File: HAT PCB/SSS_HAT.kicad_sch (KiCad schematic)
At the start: 26 parts, among them J1 ESP32_Connector_0, J2 ESP32_Connector_1, J3 CAN, J4 CAN, J5 I2C, J6 ADC_0, J7 ADC_1, SW1 I2C, SW2 IMU_SPI_Pullup, U1 TJA1051T, U2 MCP3422Axx-xMS, U3 LSM9DS1

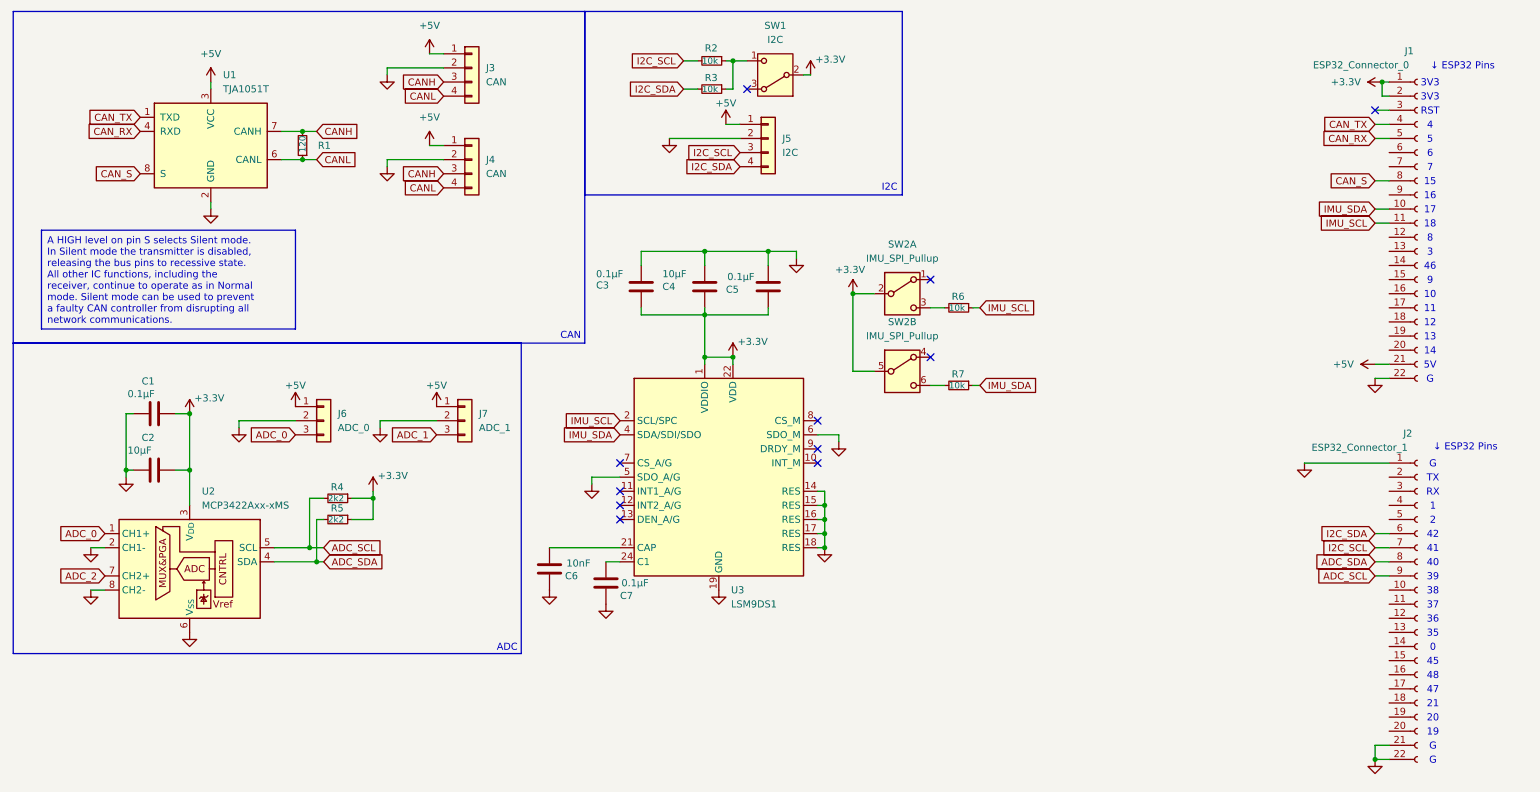
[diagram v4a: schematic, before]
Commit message: Routed PCB & Replaced IMU for ICM-42688-P
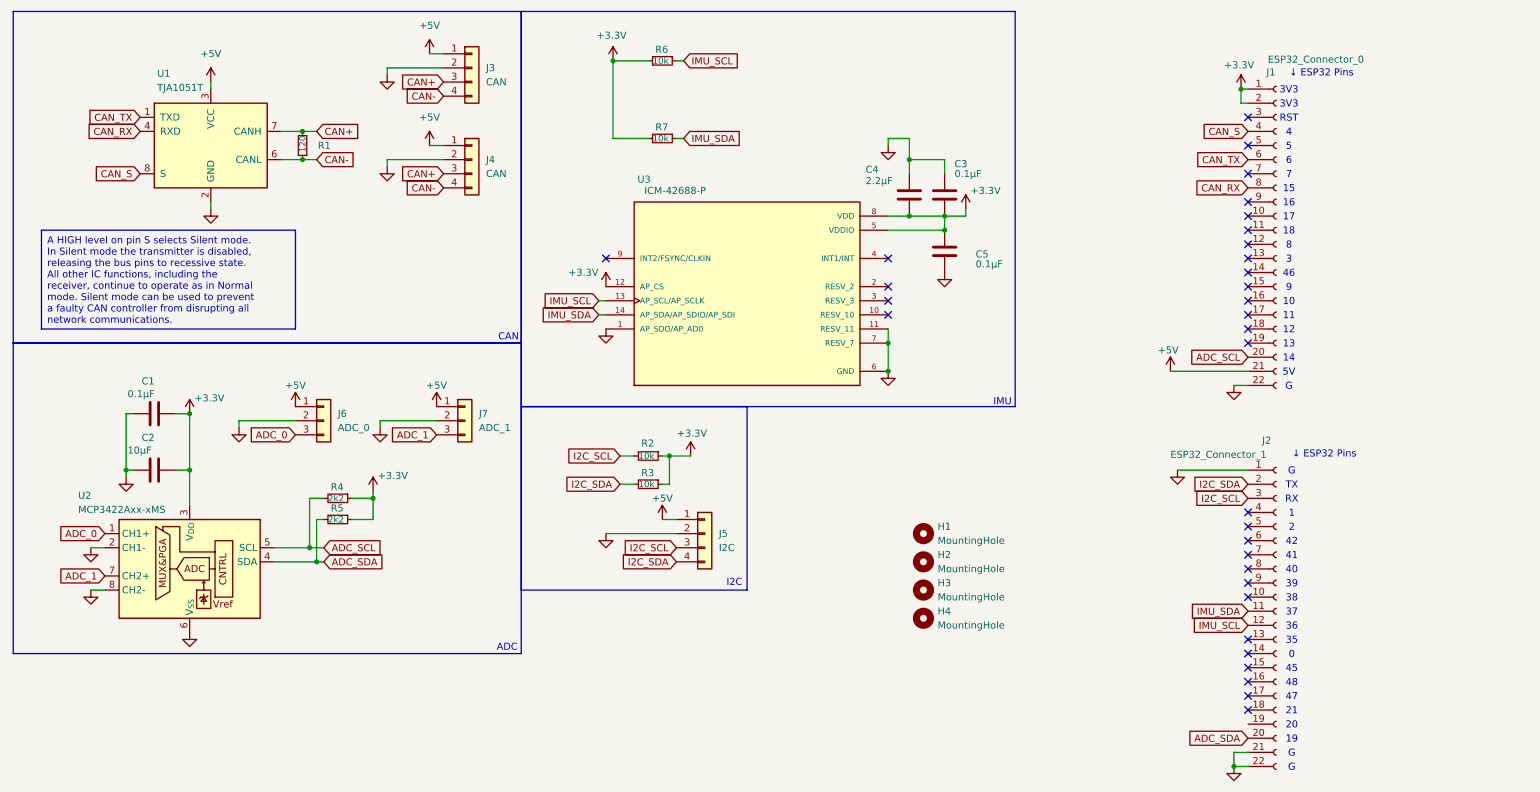
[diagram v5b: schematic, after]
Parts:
- removed C6: 10nF, Capacitor_SMD:C_0402_1005Metric_Pad0.74x0.62mm_HandSolder, symbol Device:C
- removed C7: 0.1μF, Capacitor_SMD:C_0402_1005Metric_Pad0.74x0.62mm_HandSolder, symbol Device:C
- removed SW1: I2C, Button_Switch_SMD:Nidec_Copal_CAS-120A, symbol Switch:SW_Nidec_CAS-120A1
- removed SW2: IMU_SPI_Pullup, Button_Switch_SMD:SW_DPDT_CK_JS202011JCQN, symbol Switch:SW_DPDT_x2
- removed U3: LSM9DS1, Package_LGA:LGA-24L_3x3.5mm_P0.43mm, symbol Sensor_Motion:LSM9DS1
- added H1, H2, H3, H4: MountingHole, MountingHole:MountingHole_2.7mm_M2.5, symbol Mechanical:MountingHole
- added U3: ICM-42688-P, ICM-42688-P:PQFN50P300X250X97-14N, symbol ICM-42688-P:ICM-42688-P
- C4: value 10μF -> 2.2μF
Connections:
- net ADC_2 is gone; now on net ADC_1: U2.7 (CH2+)
- net +3.3V: now also C5.1, R2.1, R3.1, R6.2, R7.2, U3.12 (AP_CS), U3.5 (VDDIO), U3.8 (VDD); no longer C5.2
- net ADC_SCL: now also J1.20 (Pin_20); no longer J2.9 (Pin_9)
- net ADC_SDA: now also J2.20 (Pin_20); no longer J2.8 (Pin_8)
- net CAN_RX: now also J1.8 (Pin_8); no longer J1.5 (Pin_5)
- net CAN_S: now also J1.4 (Pin_4); no longer J1.8 (Pin_8)
- net CAN_TX: now also J1.6 (Pin_6); no longer J1.4 (Pin_4)
- net GND: now also C5.2, U3.1 (AP_SDO/AP_AD0), U3.11 (RESV_11), U3.6 (GND), U3.7 (RESV_7); no longer C5.1
- net I2C_SCL: now also J2.3 (Pin_3); no longer J2.7 (Pin_7)
- net I2C_SDA: now also J2.2 (Pin_2); no longer J2.6 (Pin_6)
- net IMU_SCL: now also J2.12 (Pin_12), U3.13 (AP_SCL/AP_SCLK); no longer J1.11 (Pin_11)
- net IMU_SDA: now also J2.11 (Pin_11), U3.14 (AP_SDA/AP_SDIO/AP_SDI); no longer J1.10 (Pin_10)
- net CANH renamed CAN+
- net CANL renamed CAN-
- no-connect marks 11 -> 32
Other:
- note added: "IMU"
- moved on the sheet: J1, J2, R6, R7

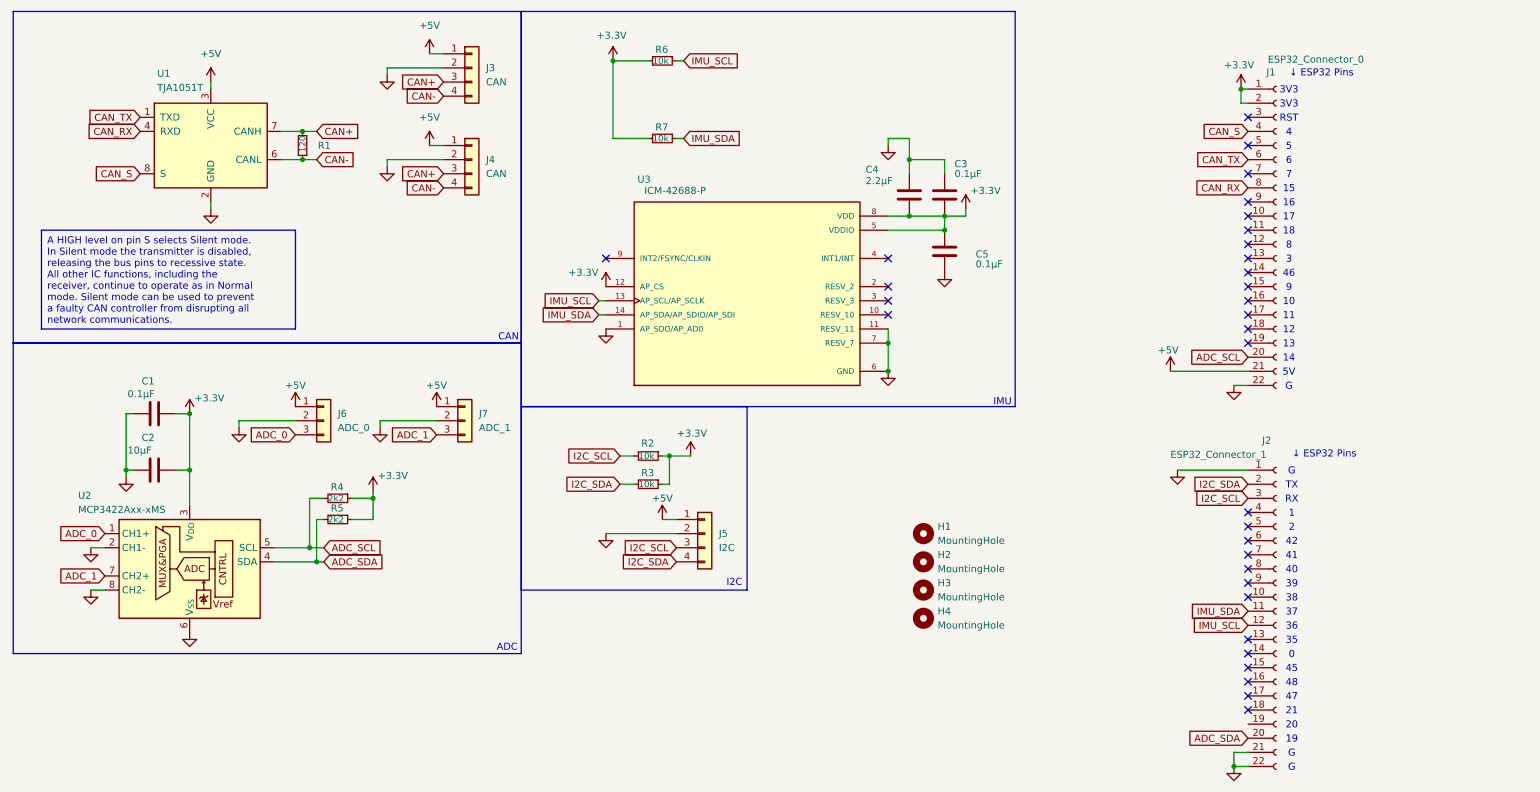
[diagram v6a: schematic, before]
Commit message: Added ADS8320EB/250 ADC
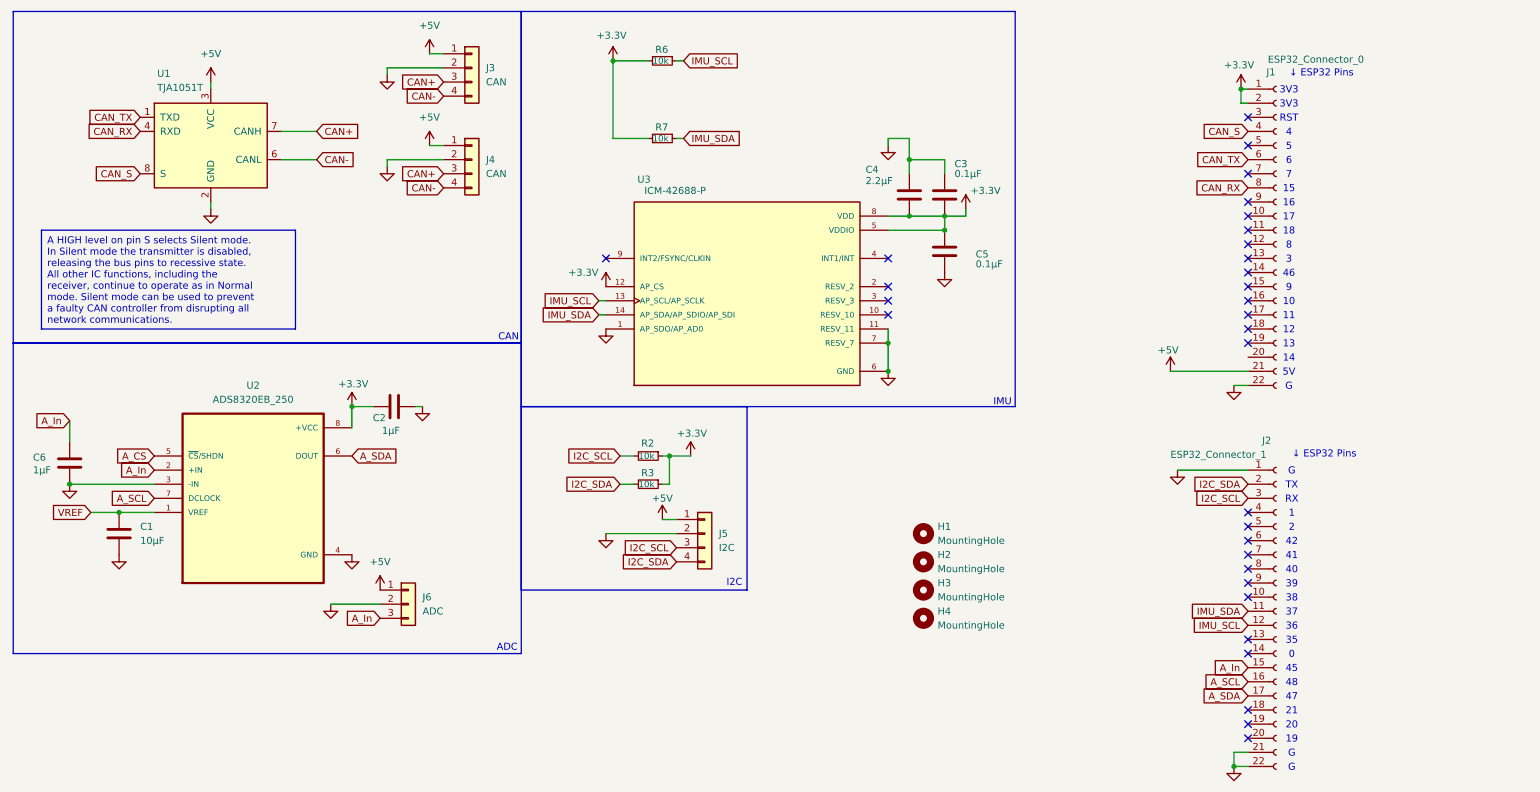
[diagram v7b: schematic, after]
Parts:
- removed J7: ADC_1, Connector_Molex:Molex_Nano-Fit_105313-xx03_1x03_P2.50mm_Horizontal, symbol Connector_Generic:Conn_01x03
- removed R1: 120, Resistor_SMD:R_0402_1005Metric_Pad0.72x0.64mm_HandSolder, symbol Device:R_Small
- removed R4, R5: 2k2, Resistor_SMD:R_0402_1005Metric_Pad0.72x0.64mm_HandSolder, symbol Device:R_Small
- removed U2: MCP3422Axx-xMS, Package_SO:MSOP-8_3x3mm_P0.65mm, symbol Analog_ADC:MCP3422Axx-xMS
- added C6: 1μF, symbol Device:C
- added U2: ADS8320EB_250, ADS8320EB_250:SOP65P490X110-8N, symbol ADS8320EB:ADS8320EB_250
- C1: value 0.1μF -> 10μF; footprint Capacitor_SMD:C_0402_1005Metric_Pad0.74x0.62mm_HandSolder -> (none)
- C2: value 10μF -> 1μF; footprint Capacitor_SMD:C_0402_1005Metric_Pad0.74x0.62mm_HandSolder -> (none)
- J6: value ADC_0 -> ADC; footprint Connector_Molex:Molex_Nano-Fit_105313-xx03_1x03_P2.50mm_Horizontal -> (none)
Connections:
- net ADC_0 is gone; now on net A_In: J6.3 (Pin_3)
- net +3.3V: now also U2.8 (+VCC); no longer C1.1
- net GND: now also C6.2, U2.3 (-IN), U2.4 (GND)
- net A_In: now reaches J2.15 (Pin_15)
- net A_In: now also C6.1, U2.2 (+IN)
- net A_SCL: now reaches J2.16 (Pin_16)
- net A_SCL: now also U2.7 (DCLOCK)
- net A_SDA: now reaches J2.17 (Pin_17)
- net A_SDA: now also U2.6 (DOUT)
- net ADC_SCL: no longer names the net of J1.20 (Pin_20)
- net ADC_SDA: no longer names the net of J2.20 (Pin_20)
- new net A_CS: U2.5 (~{CS}/SHDN)
- new net VREF: C1.1, U2.1 (VREF)
- no-connect marks 32 -> 31

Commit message: Updated 3D model & readme.
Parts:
- removed J3, J4: CAN, Connector_Molex:Molex_Nano-Fit_105313-xx04_1x04_P2.50mm_Horizontal, symbol Connector_Generic:Conn_01x04
- removed J5: I2C, Connector_Molex:Molex_Nano-Fit_105313-xx04_1x04_P2.50mm_Horizontal, symbol Connector_Generic:Conn_01x04
- removed J6: ADC, symbol Connector_Generic:Conn_01x03
- removed R6, R7: 10k, Resistor_SMD:R_0402_1005Metric_Pad0.72x0.64mm_HandSolder, symbol Device:R_Small
- added J3, J4, J5: I2C, Connector_Hirose:Hirose_DF3EA-04P-2H_1x04-1MP_P2.00mm_Horizontal, symbol Connector_Generic_MountingPin:Conn_01x04_MountingPin
- added J6: ADC, Connector_Hirose:Hirose_DF3EA-03P-2H_1x03-1MP_P2.00mm_Horizontal, symbol Connector_Generic_MountingPin:Conn_01x03_MountingPin
- C1, C2, C6: footprint (none) -> Capacitor_SMD:C_0402_1005Metric_Pad0.74x0.62mm_HandSolder
- U2: footprint ADS8320EB_250:SOP65P490X110-8N -> ADS8320EB_250:DGK0008A_L
- renumbered R2 to R1, R3 to R2
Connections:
- net VREF is gone; now on net +3.3V: C1.1, U2.1 (VREF)
- net +3.3V: no longer U3.12 (AP_CS)
- net +5V: now also J3.1 (Pin_1), J4.1 (Pin_1), J5.1 (Pin_1), J6.1 (Pin_1)
- net A_CS: now also J2.7 (Pin_7)
- net A_In: now also J2.4 (Pin_4), J6.3 (Pin_3); no longer J2.15 (Pin_15)
- net A_SCL: now also J2.5 (Pin_5); no longer J2.16 (Pin_16)
- net A_SDA: now also J2.6 (Pin_6); no longer J2.17 (Pin_17)
- net CAN+: now also J3.4 (Pin_4), J4.4 (Pin_4)
- net CAN-: now also J3.3 (Pin_3), J4.3 (Pin_3)
- net CAN_RX: now also J1.17 (Pin_17); no longer J1.8 (Pin_8)
- net CAN_S: now also J1.18 (Pin_18); no longer J1.4 (Pin_4)
- net CAN_TX: now also J1.16 (Pin_16); no longer J1.6 (Pin_6)
- net GND: now also J3.2 (Pin_2), J3.MP (MountPin), J4.2 (Pin_2), J4.MP (MountPin), J5.2 (Pin_2), J5.MP (MountPin), J6.2 (Pin_2), J6.MP (MountPin); no longer U3.1 (AP_SDO/AP_AD0)
- net I2C_SCL: now also J1.5 (Pin_5), J5.3 (Pin_3); no longer J2.3 (Pin_3)
- net I2C_SDA: now also J1.4 (Pin_4), J5.4 (Pin_4); no longer J2.2 (Pin_2)
- net IMU_INT1: now reaches J1.11 (Pin_11)
- net IMU_INT1: now also U3.4 (INT1/INT)
- net IMU_INT2: now reaches J1.12 (Pin_12)
- net IMU_INT2: now also U3.9 (INT2/FSYNC/CLKIN)
- net IMU_MISO: now reaches J2.10 (Pin_10)
- net IMU_MISO: now also U3.1 (AP_SDO/AP_AD0)
- net IMU_CS: now reaches J2.13 (Pin_13)
- net IMU_CS: now also U3.12 (AP_CS)
- net IMU_SDA renamed IMU_MOSI
- no-connect marks 31 -> 25
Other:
- moved on the sheet: C3, C4, C5, H1, H2, H3, H4, U3
